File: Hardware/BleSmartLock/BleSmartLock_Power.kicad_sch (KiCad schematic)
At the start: 28 parts, among them J1 Conn_01x02, J2 Conn_01x01, J3 Conn_01x01, J4 Conn_01x01, Q1 PMV50UPE, Q2 PMV50UPE, U1 RT9086, U2 XC9264b755

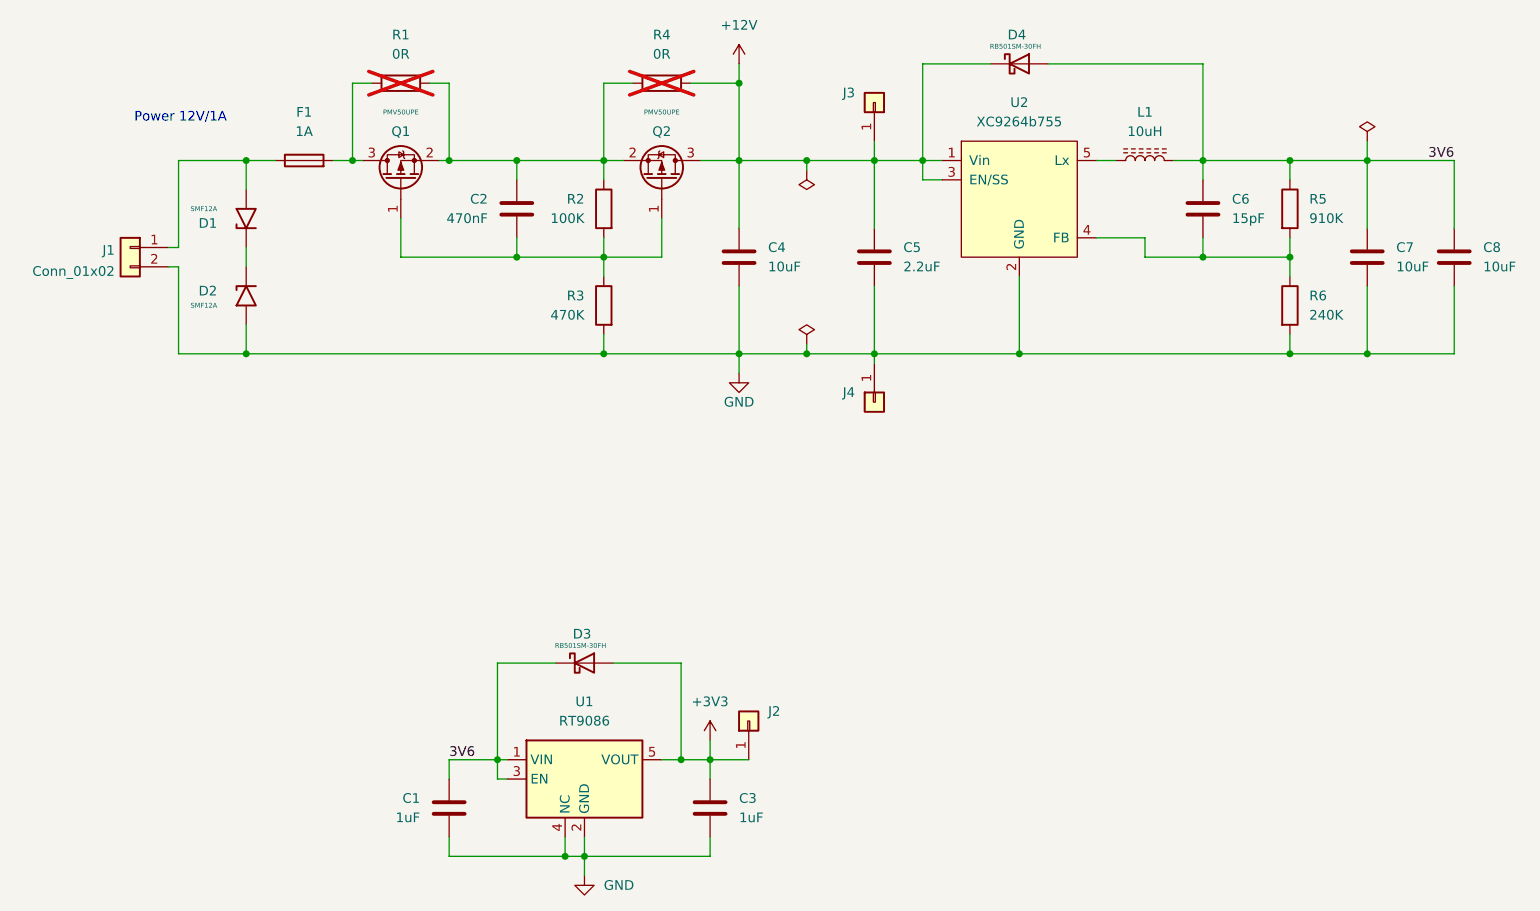
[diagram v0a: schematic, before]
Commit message: Ajout carte BleSmartLock
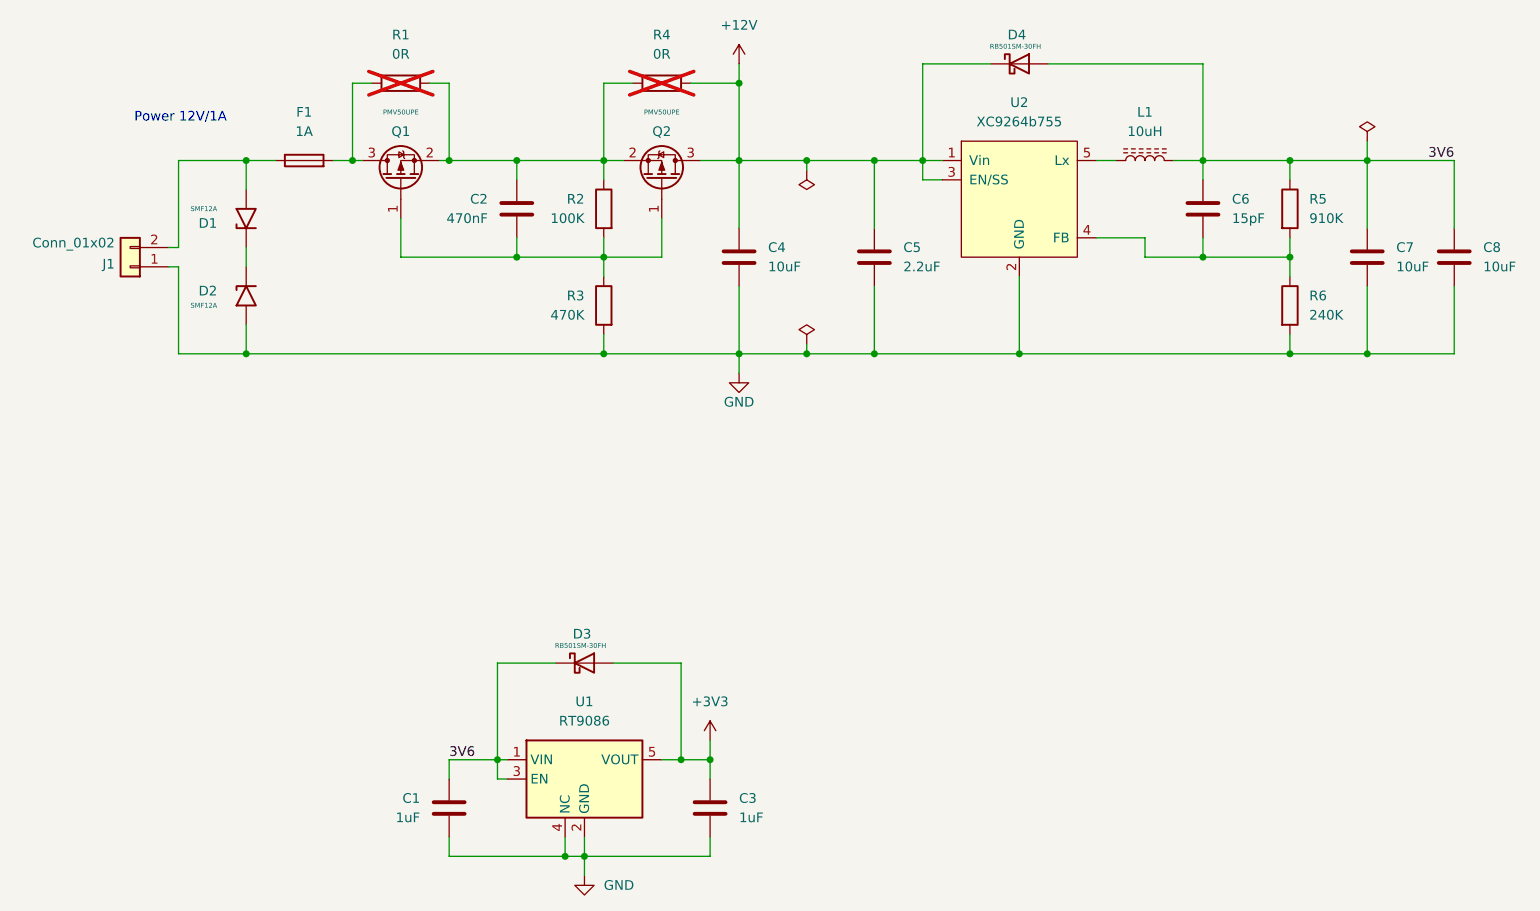
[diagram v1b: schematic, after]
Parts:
- removed J2, J3, J4: Conn_01x01, Connector_PinHeader_2.54mm:PinHeader_1x01_P2.54mm_Vertical, symbol Connector_Generic:Conn_01x01
- L1: footprint AM163:L_TDK_VLS252012HBX_Handsoldering -> Inductor_SMD:L_1008_2520Metric_Pad1.43x2.20mm_HandSolder
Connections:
- net GND: now also J1.1 (Pin_1); no longer J1.2 (Pin_2)
- net at D1.2 (A2), F1.1: now also J1.2 (Pin_2); no longer J1.1 (Pin_1)
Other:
- company: (none) -> antoine163
- title: (none) -> Ble Smart Lock
- moved on the sheet: J1

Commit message: Ajout fichier de production et bom interactive
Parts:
- U2: Vendor (none) -> Torex:XC9264b755
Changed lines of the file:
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@@
+			)
+		)
+		(property "Vendor" "Torex:XC9264b755"
+			(at 172.72 63.5 0)
+			(effects
+				(font
+					(size 1.27 1.27)
+				)
+				(hide yes)
 			)
 		)
